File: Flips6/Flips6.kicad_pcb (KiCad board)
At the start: 2 copper layers, 100 x 50 mm, 25 parts, among them CN1 Conn_02x04_Odd_Even, IC1 74595, IC2 74595, IC3 74595

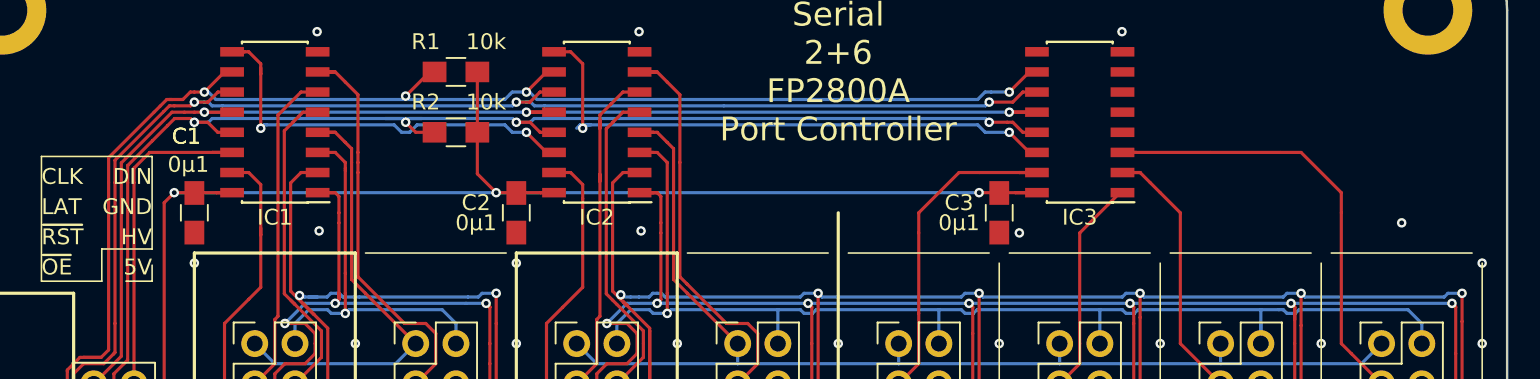
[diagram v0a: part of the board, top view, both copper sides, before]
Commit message: adding pinout of CNX/CNY connectors
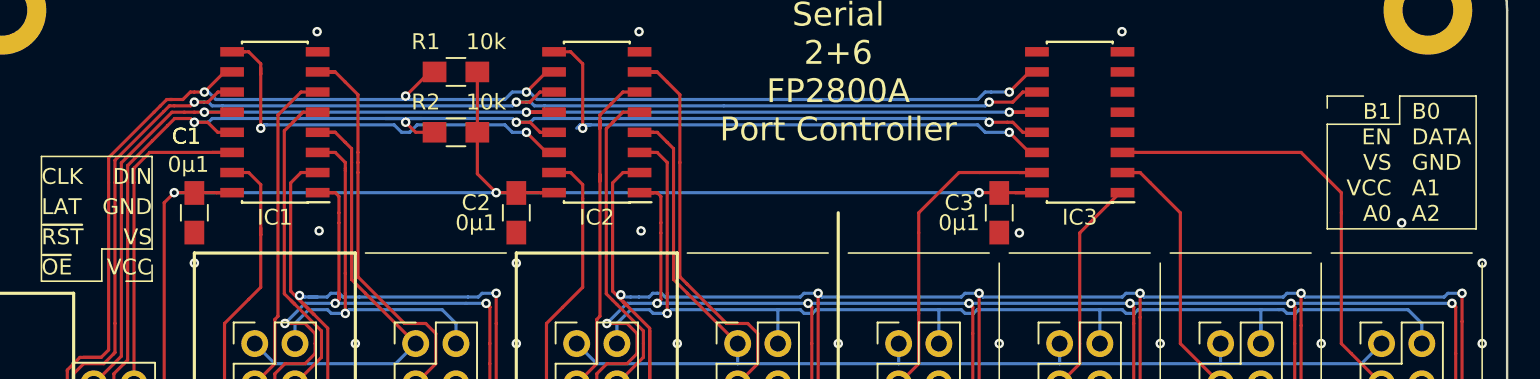
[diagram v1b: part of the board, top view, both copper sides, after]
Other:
- board text added: ".0 Y.A0 X.A0 X3.EN"
- board text added: ".1 Y.A1 X.A1 X4.EN"
- board text added: ".2 Y.A2 X.A2 X5.EN"
- board text added: ".3 Y.B0 X.B0 X6.EN"
- board text added: ".4 Y.B1 X.B1"
- board text added: ".5 Y.DAT X.DAT"
- board text added: ".6 Y1.EN X1.EN"
- board text added: ".7 Y2.EN X2.EN"
- board text added: "0. 1. 2."
- board text added: "B0 DATA GND A1 A2"
- board text added: "B1 EN VS VCC A0"
- board text added: "VCC"
- board text added: "VS"
- board text removed: "0 1 2"
- board text removed: "0 Y.A0 X.A0 X3.EN"
- board text removed: "1 Y.A1 X.A1 X4.EN"
- board text removed: "2 Y.A2 X.A2 X5.EN"
- board text removed: "3 Y.B0 X.B0 X6.EN"
- board text removed: "4 Y.B1 X.B1"
- board text removed: "5 Y.DAT X.DAT"
- board text removed: "5V"
- board text removed: "6 Y1.EN X1.EN"
- board text removed: "7 Y2.EN X2.EN"
- board text removed: "HV"
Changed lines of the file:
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@@
   (general
     (thickness 1.6)
-    (drawings 92)
+    (drawings 102)
     (tracks 791)
     (zones 0)
@@
     (last_trace_width 0.2)
     (trace_clearance 0.2)
-    (zone_clearance 0.1524)
+    (zone_clearance 0.2)
     (zone_45_only no)
     (trace_min 0.2)
@@
     )
   )
+  (gr_line (start 139.446 61.214) (end 139.446 61.976) (layer F.SilkS) (width 0.1))
+  (gr_line (start 139.446 61.214) (end 141.732 61.214) (layer F.SilkS) (width 0.1))
+  (gr_line (start 148.844 61.214) (end 148.844 69.596) (layer F.SilkS) (width 0.1))
+  (gr_line (start 144.018 61.214) (end 148.844 61.214) (layer F.SilkS) (width 0.1))
+  (gr_line (start 144.018 62.992) (end 144.018 61.214) (layer F.SilkS) (width 0.1))
+  (gr_line (start 139.446 62.992) (end 144.018 62.992) (layer F.SilkS) (width 0.1))
+  (gr_line (start 139.446 69.596) (end 139.446 62.992) (layer F.SilkS) (width 0.1))
+  (gr_line (start 148.844 69.596) (end 139.446 69.596) (layer F.SilkS) (width 0.1))
+  (gr_text "B0\nDATA\nGND\nA1\nA2" (at 144.78 65.405) (layer F.SilkS)
+    (effects (font (size 1 1) (thickness 0.15)) (justify left))
+  )
+  (gr_text "B1\nEN\nVS\nVCC\nA0" (at 143.51 65.405) (layer F.SilkS)
+    (effects (font (size 1 1) (thickness 0.15)) (justify right))
+  )
   (gr_line (start 126.365 66.04) (end 126.365 68.58) (layer B.SilkS) (width 0.1))
   (gr_line (start 118.745 66.04) (end 118.745 68.58) (layer B.SilkS) (width 0.1))
@@
     (effects (font (size 1.5 1.5) (thickness 0.3)) (justify left mirror))
   )
-  (gr_text "7\nY2.EN\nX2.EN\n " (at 80.01 63.5) (layer B.SilkS)
+  (gr_text ".7\nY2.EN\nX2.EN\n " (at 80.01 63.5) (layer B.SilkS)
     (effects (font (size 1.5 1.5) (thickness 0.3)) (justify left mirror))
   )
-  (gr_text "6   \nY1.EN\nX1.EN\n " (at 87.63 63.5) (layer B.SilkS)
+  (gr_text ".6   \nY1.EN\nX1.EN\n " (at 87.63 63.5) (layer B.SilkS)
     (effects (font (size 1.5 1.5) (thickness 0.3)) (justify left mirror))
   )
-  (gr_text "5   \nY.DAT\nX.DAT\n " (at 95.25 63.5) (layer B.SilkS)
+  (gr_text ".5   \nY.DAT\nX.DAT\n " (at 95.25 63.5) (layer B.SilkS)
     (effects (font (size 1.5 1.5) (thickness 0.3)) (justify left mirror))
   )
-  (gr_text "4   \nY.B1\nX.B1\n " (at 102.87 63.5) (layer B.SilkS)
+  (gr_text ".4   \nY.B1\nX.B1\n " (at 102.87 63.5) (layer B.SilkS)
     (effects (font (size 1.5 1.5) (thickness 0.3)) (justify left mirror))
   )
-  (gr_text "3   \nY.B0\nX.B0\nX6.EN" (at 110.49 63.5) (layer B.SilkS)
+  (gr_text ".3   \nY.B0\nX.B0\nX6.EN" (at 110.49 63.5) (layer B.SilkS)
     (effects (font (size 1.5 1.5) (thickness 0.3)) (justify left mirror))
   )
-  (gr_text "2   \nY.A2\nX.A2\nX5.EN" (at 118.11 63.5) (layer B.SilkS)
+  (gr_text ".2   \nY.A2\nX.A2\nX5.EN" (at 118.11 63.5) (layer B.SilkS)
     (effects (font (size 1.5 1.5) (thickness 0.3)) (justify left mirror))
   )
-  (gr_text "1   \nY.A1\nX.A1\nX4.EN" (at 125.73 63.5) (layer B.SilkS)
+  (gr_text ".1   \nY.A1\nX.A1\nX4.EN" (at 125.73 63.5) (layer B.SilkS)
     (effects (font (size 1.5 1.5) (thickness 0.3)) (justify left mirror))
   )
-  (gr_text "0   \nY.A0\nX.A0\nX3.EN" (at 133.35 63.5) (layer B.SilkS)
+  (gr_text ".0   \nY.A0\nX.A0\nX3.EN" (at 133.35 63.5) (layer B.SilkS)
     (effects (font (size 1.5 1.5) (thickness 0.3)) (justify left mirror))
   )
-  (gr_text "\n0\n1\n2" (at 137.795 63.5) (layer B.SilkS)
+  (gr_text "\n0.\n1.\n2." (at 137.795 63.5) (layer B.SilkS)
     (effects (font (size 1.5 1.5) (thickness 0.3)) (justify left mirror))
   )
@@
     (effects (font (size 1 1) (thickness 0.15)) (justify right))
   )
-  (gr_text HV (at 65.278 70.104) (layer F.SilkS)
+  (gr_text VS (at 65.278 70.104) (layer F.SilkS)
     (effects (font (size 1 1) (thickness 0.15)) (justify right))
   )
-  (gr_text 5V (at 65.278 72.009) (layer F.SilkS)
+  (gr_text VCC (at 65.278 72.009) (layer F.SilkS)
     (effects (font (size 1 1) (thickness 0.15)) (justify right))
   )
@@
   (segment (start 127.381 64.77) (end 126.525 64.77) (width 0.2) (layer F.Cu) (net 30) (status 800000))
   (zone (net 2) (net_name GND) (layer F.Cu) (hatch edge 0.508)
-    (connect_pads (clearance 0.1524))
-    (min_thickness 0.1524)
-    (fill yes (arc_segments 16) (thermal_gap 0.25) (thermal_bridge_width 0.508))
+    (connect_pads (clearance 0.2))
+    (min_thickness 0.2)
+    (fill yes (arc_segments 32) (thermal_gap 0.2) (thermal_bridge_width 0.508))
     (polygon
       (pts
@@
   )
   (zone (net 2) (net_name GND) (layer B.Cu) (hatch edge 0.508)
-    (connect_pads (clearance 0.1524))
-    (min_thickness 0.1524)
-    (fill yes (arc_segments 16) (thermal_gap 0.25) (thermal_bridge_width 0.508))
+    (connect_pads (clearance 0.2))
+    (min_thickness 0.2)
+    (fill yes (arc_segments 32) (thermal_gap 0.2) (thermal_bridge_width 0.508))
     (polygon
       (pts

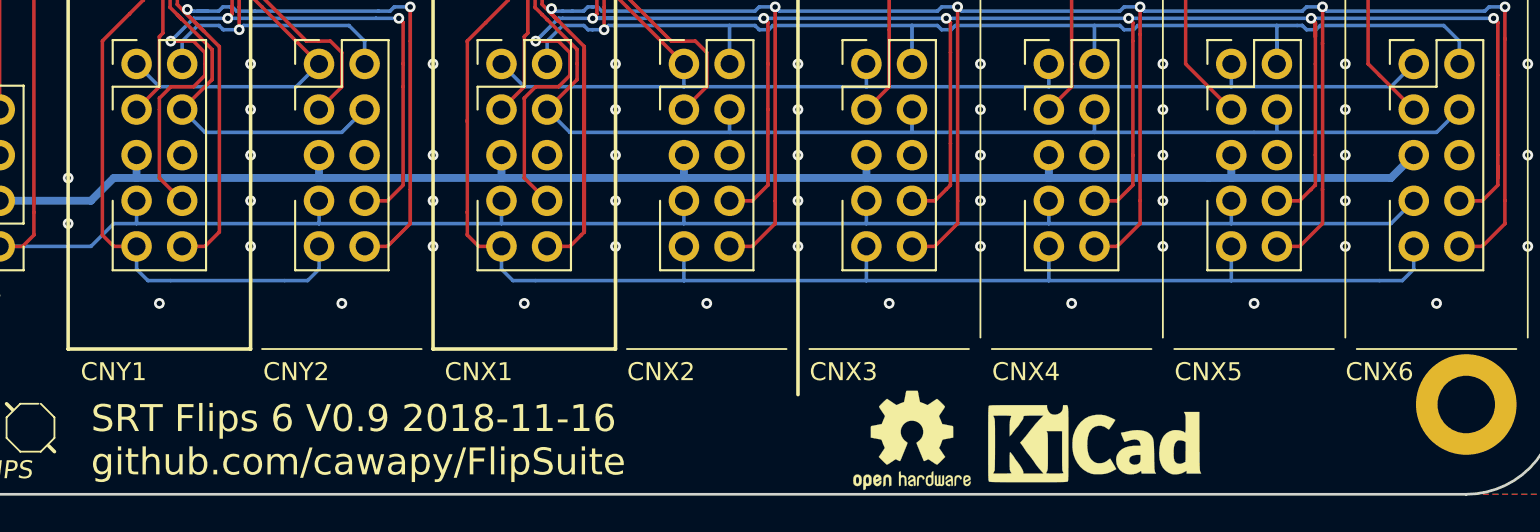
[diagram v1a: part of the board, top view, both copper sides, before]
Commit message: adding pulldowns for enable pins
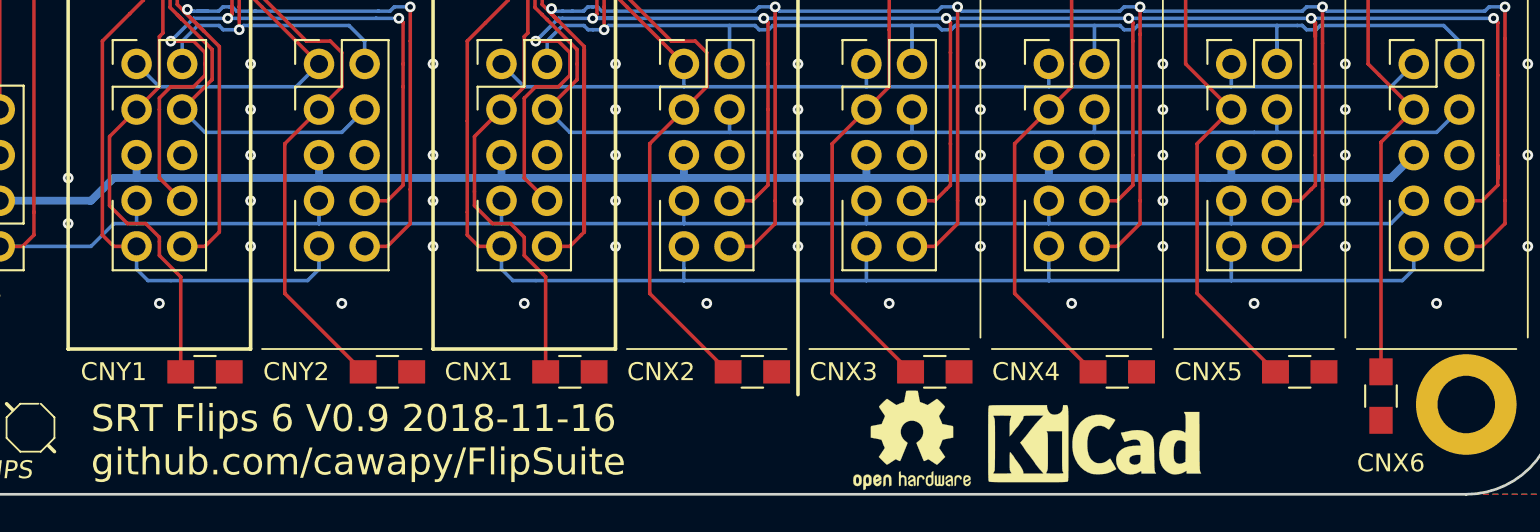
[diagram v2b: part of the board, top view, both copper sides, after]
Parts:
- added R10: 10k, Resistors_SMD:R_0805_HandSoldering, F.Cu at (141.1, 95.3)
- added R3: 10k, Resistors_SMD:R_0805_HandSoldering, F.Cu at (75.6, 94.0)
- added R4: 10k, Resistors_SMD:R_0805_HandSoldering, F.Cu at (85.7, 94.0)
- added R5: 10k, Resistors_SMD:R_0805_HandSoldering, F.Cu at (95.9, 94.0)
- added R6: 10k, Resistors_SMD:R_0805_HandSoldering, F.Cu at (106.0, 94.0)
- added R7: 10k, Resistors_SMD:R_0805_HandSoldering, F.Cu at (116.2, 94.0)
- added R8: 10k, Resistors_SMD:R_0805_HandSoldering, F.Cu at (126.4, 94.0)
- added R9: 10k, Resistors_SMD:R_0805_HandSoldering, F.Cu at (136.5, 94.0)
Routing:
- net /YEN1: track 21.1 -> 38.6 mm
- net /XEN1: track 21.6 -> 39.1 mm
- net /XEN3: track 20.5 -> 37.7 mm
- net /XEN5: track 17.2 -> 34.4 mm
- net /YEN2: track 25.4 -> 42.6 mm
- net /XEN4: track 13.8 -> 31.0 mm
- net /XEN2: track 26.0 -> 43.2 mm
- net /XEN6: track 28.4 -> 43.7 mm

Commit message: Prepare release
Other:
- board text added: "SRT Flips 6 V1.0 2018-11-23 github.com/cawapy/FlipSuite"
- board text removed: "SRT Flips 6 V0.9 2018-11-16 github.com/cawapy/FlipSuite"
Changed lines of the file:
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@@
   (title_block
     (title "Flips 6")
-    (date 2018-11-16)
-    (rev V0.9)
+    (date 2018-11-23)
+    (rev V1.0)
     (company SRT)
     (comment 1 "Serial 2+6 FP2800A Port Controller")
@@
     (last_trace_width 0.2)
     (trace_clearance 0.2)
-    (zone_clearance 0.2)
+    (zone_clearance 0.16)
     (zone_45_only no)
     (trace_min 0.2)
@@
     (pad 6 thru_hole oval (at 2.54 5.08 180) (size 1.7 1.7) (drill 1) (layers *.Cu *.Mask)
       (net 6 /SRCLK))
-    (pad 5 thru_hole oval (at 0 5.08 180) (size 1.7 1.7) (drill 1) (layers *.Cu *.Mask)
+    (pad 5 thru_hole oval (at 0 5.08 225) (size 1.7 1.7) (drill 1) (layers *.Cu *.Mask)
       (net 2 GND))
     (pad 4 thru_hole oval (at 2.54 2.54 180) (size 1.7 1.7) (drill 1) (layers *.Cu *.Mask)
@@
   (gr_line (start 109.22 71.12) (end 118.11 71.12) (layer F.SilkS) (width 0.1))
   (gr_line (start 119.38 71.12) (end 128.27 71.12) (layer F.SilkS) (width 0.1))
-  (gr_text "SRT Flips 6 V0.9 2018-11-16\ngithub.com/cawapy/FlipSuite" (at 69.215 97.79) (layer F.SilkS)
+  (gr_text "SRT Flips 6 V1.0 2018-11-23\ngithub.com/cawapy/FlipSuite" (at 69.215 97.79) (layer F.SilkS)
     (effects (font (size 1.5 1.5) (thickness 0.3)) (justify left))
   )
